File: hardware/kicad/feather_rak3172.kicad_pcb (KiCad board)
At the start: 2 copper layers, 51 x 23.1 mm, 51 parts, among them J1 Pin Header, J2 Pin Header, J3 USB_C_Receptacle_USB2.0, J4 915MHz SMA, J5 SWD, J6 JST-2PH, Q1 DMG341, SW1 RESET, SW2 BOOT, U1 RAK3172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

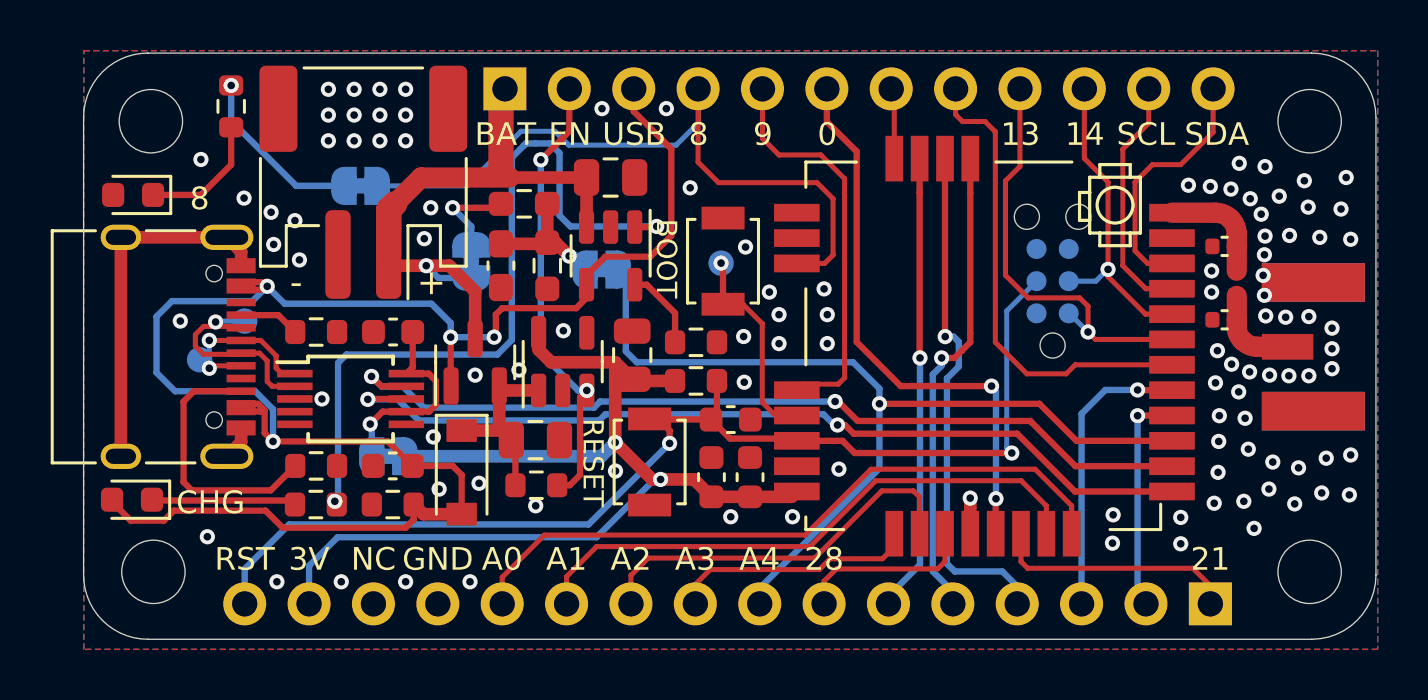
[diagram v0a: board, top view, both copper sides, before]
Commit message: minor traces adjustment
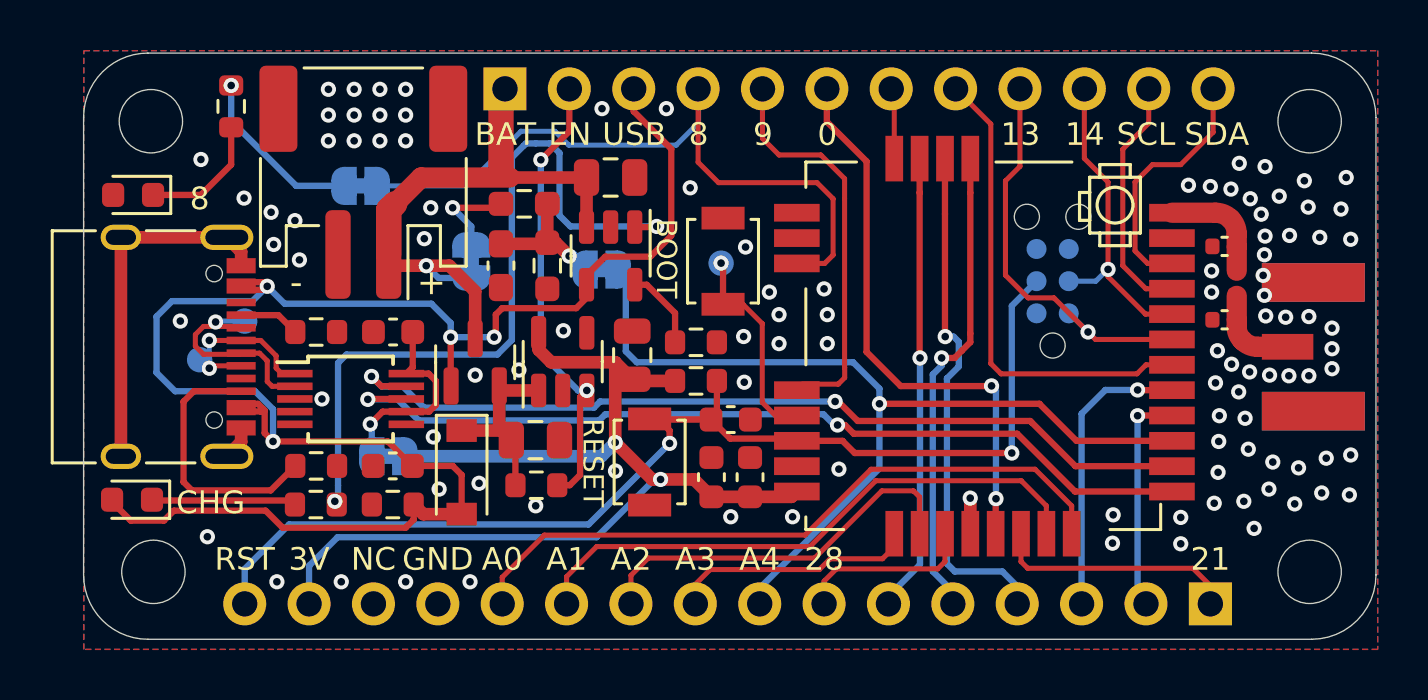
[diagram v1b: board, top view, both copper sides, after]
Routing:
- net /PA13: track 16.9 -> 16.3 mm
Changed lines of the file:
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@@
   (via (at 139.954 106.172) (size 0.6) (drill 0.3) (layers "F.Cu" "B.Cu") (net 13))
   (via (at 153.4563 106.553) (size 0.6) (drill 0.3) (layers "F.Cu" "B.Cu") (net 13))
-  (segment (start 153.25632 100.94688) (end 153.25632 106.35302) (width 0.2) (layer "B.Cu") (net 13))
+  (segment (start 153.4563 106.553) (end 153.4563 100.7469) (width 0.25) (layer "B.Cu") (net 13))
   (segment (start 124.94452 109.37048) (end 123.19 111.125) (width 0.25) (layer "B.Cu") (net 13))
-  (segment (start 154.432 99.7712) (end 153.25632 100.94688) (width 0.2) (layer "B.Cu") (net 13))
   (segment (start 123.19 111.125) (end 123.19 112.503949) (width 0.25) (layer "B.Cu") (net 13))
   (segment (start 139.954 106.172) (end 136.75552 109.37048) (width 0.25) (layer "B.Cu") (net 13))
   (segment (start 136.75552 109.37048) (end 124.94452 109.37048) (width 0.25) (layer "B.Cu") (net 13))
-  (segment (start 153.25632 106.35302) (end 153.4563 106.553) (width 0.2) (layer "B.Cu") (net 13))
+  (segment (start 153.4563 100.7469) (end 154.432 99.7712) (width 0.25) (layer "B.Cu") (net 13))
   (segment (start 162.3314 101.5873) (end 162.3314 101.31316) (width 0.8) (layer "F.Cu") (net 14))
   (segment (start 163.155249 102.362) (end 164.338 102.362) (width 0.8) (layer "F.Cu") (net 14))
@@
   (segment (start 157.0736 99.4706) (end 157.090399 99.4706) (width 0.2) (layer "B.Cu") (net 43))
   (segment (start 157.090399 99.4706) (end 157.253999 99.307) (width 0.2) (layer "B.Cu") (net 43))
+  (segment (start 156.464 101.7778) (end 155.1178 100.4316) (width 0.2) (layer "F.Cu") (net 44))
   (segment (start 156.464 101.7778) (end 156.7578 102.0716) (width 0.2) (layer "F.Cu") (net 44))
+  (segment (start 154.1018 100.4316) (end 153.206179 99.535979) (width 0.2) (layer "F.Cu") (net 44))
+  (segment (start 153.778949 95.242651) (end 153.778949 92.183949) (width 0.2) (layer "F.Cu") (net 44))
   (segment (start 153.206179 95.815421) (end 153.778949 95.242651) (width 0.2) (layer "F.Cu") (net 44))
-  (segment (start 153.206179 99.535979) (end 153.206179 99.358179) (width 0.2) (layer "F.Cu") (net 44))
-  (segment (start 156.464 100.7618) (end 156.1338 100.4316) (width 0.2) (layer "F.Cu") (net 44))
-  (segment (start 154.1018 100.4316) (end 153.206179 99.535979) (width 0.2) (layer "F.Cu") (net 44))
-  (segment (start 156.1338 100.4316) (end 154.1018 100.4316) (width 0.2) (layer "F.Cu") (net 44))
   (segment (start 156.7578 102.0716) (end 159.7746 102.0716) (width 0.2) (layer "F.Cu") (net 44))
-  (segment (start 156.464 101.7778) (end 156.464 100.7618) (width 0.2) (layer "F.Cu") (net 44))
-  (segment (start 153.206179 99.358179) (end 153.206179 95.815421) (width 0.2) (layer "F.Cu") (net 44))
-  (segment (start 153.778949 95.242651) (end 153.778949 92.183949) (width 0.2) (layer "F.Cu") (net 44))
+  (segment (start 153.206179 99.535979) (end 153.206179 95.815421) (width 0.2) (layer "F.Cu") (net 44))
+  (segment (start 155.1178 100.4316) (end 154.1018 100.4316) (width 0.2) (layer "F.Cu") (net 44))
   (via (at 156.464 101.7778) (size 0.6) (drill 0.3) (layers "F.Cu" "B.Cu") (net 44))
   (segment (start 155.7274 101.0412) (end 156.464 101.7778) (width 0.2) (layer "B.Cu") (net 44))
@@
   (segment (start 154.0826 111.0996) (end 160.6042 111.0996) (width 0.2) (layer "F.Cu") (net 47))
   (segment (start 160.6042 111.0996) (end 161.29 111.7854) (width 0.2) (layer "F.Cu") (net 47))
-  (segment (start 155.6004 103.4288) (end 154.051 103.4288) (width 0.2) (layer "F.Cu") (net 48))
-  (segment (start 151.511 93.472) (end 151.238949 93.199949) (width 0.2) (layer "F.Cu") (net 48))
-  (segment (start 152.806659 93.878659) (end 152.4 93.472) (width 0.2) (layer "F.Cu") (net 48))
-  (segment (start 152.806659 102.184459) (end 152.806659 93.878659) (width 0.2) (layer "F.Cu") (net 48))
-  (segment (start 154.051 103.4288) (end 152.806659 102.184459) (width 0.2) (layer "F.Cu") (net 48))
-  (segment (start 155.9576 103.0716) (end 155.6004 103.4288) (width 0.2) (layer "F.Cu") (net 48))
-  (segment (start 152.4 93.472) (end 151.511 93.472) (width 0.2) (layer "F.Cu") (net 48))
-  (segment (start 159.7746 103.0716) (end 155.9576 103.0716) (width 0.2) (layer "F.Cu") (net 48))
-  (segment (start 151.238949 93.199949) (end 151.238949 92.183949) (width 0.2) (layer "F.Cu") (net 48))
+  (segment (start 152.6286 93.5736) (end 151.238949 92.183949) (width 0.2) (layer "F.Cu") (net 48))
+  (segment (start 152.6286 103.0224) (end 152.6286 93.5736) (width 0.2) (layer "F.Cu") (net 48))
+  (segment (start 158.7516 103.0716) (end 158.3944 103.4288) (width 0.2) (layer "F.Cu") (net 48))
+  (segment (start 153.035 103.4288) (end 152.6286 103.0224) (width 0.2) (layer "F.Cu") (net 48))
+  (segment (start 159.7746 103.0716) (end 158.7516 103.0716) (width 0.2) (layer "F.Cu") (net 48))
+  (segment (start 158.3944 103.4288) (end 153.035 103.4288) (width 0.2) (layer "F.Cu") (net 48))
   (segment (start 148.8196 92.3046) (end 148.698949 92.183949) (width 0.2) (layer "F.Cu") (net 49))
   (segment (start 148.8196 94.9366) (end 148.8196 92.3046) (width 0.2) (layer "F.Cu") (net 49))
-  (segment (start 147.33764 102.17644) (end 149.0726 103.9114) (width 0.25) (layer "F.Cu") (net 50))
-  (segment (start 147.33764 94.65804) (end 147.33764 102.17644) (width 0.25) (layer "F.Cu") (net 50))
+  (segment (start 152.648133 103.9114) (end 149.0726 103.9114) (width 0.25) (layer "F.Cu") (net 50))
   (segment (start 152.8196 109.7366) (end 152.8196 108.3686) (width 0.25) (layer "F.Cu") (net 50))
+  (segment (start 149.0726 103.9114) (end 147.7264 102.5652) (width 0.25) (layer "F.Cu") (net 50))
+  (segment (start 146.158949 93.479349) (end 146.158949 92.183949) (width 0.25) (layer "F.Cu") (net 50))
   (segment (start 152.8196 108.3686) (end 152.8318 108.3564) (width 0.25) (layer "F.Cu") (net 50))
-  (segment (start 146.158949 92.183949) (end 146.158949 93.479349) (width 0.25) (layer "F.Cu") (net 50))
-  (segment (start 146.158949 93.479349) (end 147.33764 94.65804) (width 0.25) (layer "F.Cu") (net 50))
-  (segment (start 149.0726 103.9114) (end 152.65682 103.9114) (width 0.25) (layer "F.Cu") (net 50))
-  (via (at 152.65682 103.9114) (size 0.6) (drill 0.3) (layers "F.Cu" "B.Cu") (net 50))
+  (segment (start 152.65682 103.902713) (end 152.648133 103.9114) (width 0.25) (layer "F.Cu") (net 50))
+  (segment (start 147.7264 95.0468) (end 146.158949 93.479349) (width 0.25) (layer "F.Cu") (net 50))
+  (segment (start 147.7264 102.5652) (end 147.7264 95.0468) (width 0.25) (layer "F.Cu") (net 50))
+  (via (at 152.65682 103.902713) (size 0.6) (drill 0.3) (layers "F.Cu" "B.Cu") (net 50))
   (via (at 152.8318 108.3564) (size 0.6) (drill 0.3) (layers "F.Cu" "B.Cu") (net 50))
-  (segment (start 152.8318 104.08638) (end 152.65682 103.9114) (width 0.25) (layer "B.Cu") (net 50))
-  (segment (start 152.8318 108.3564) (end 152.8318 104.08638) (width 0.25) (layer "B.Cu") (net 50))
+  (segment (start 152.8318 104.077693) (end 152.8318 108.3564) (width 0.25) (layer "B.Cu") (net 50))
+  (segment (start 152.65682 103.902713) (end 152.8318 104.077693) (width 0.25) (layer "B.Cu") (net 50))
   (segment (start 146.8628 103.5812) (end 146.6088 103.8352) (width 0.2) (layer "F.Cu") (net 51))
   (segment (start 146.8628 103.18216) (end 146.8628 103.5812) (width 0.2) (layer "F.Cu") (net 51))

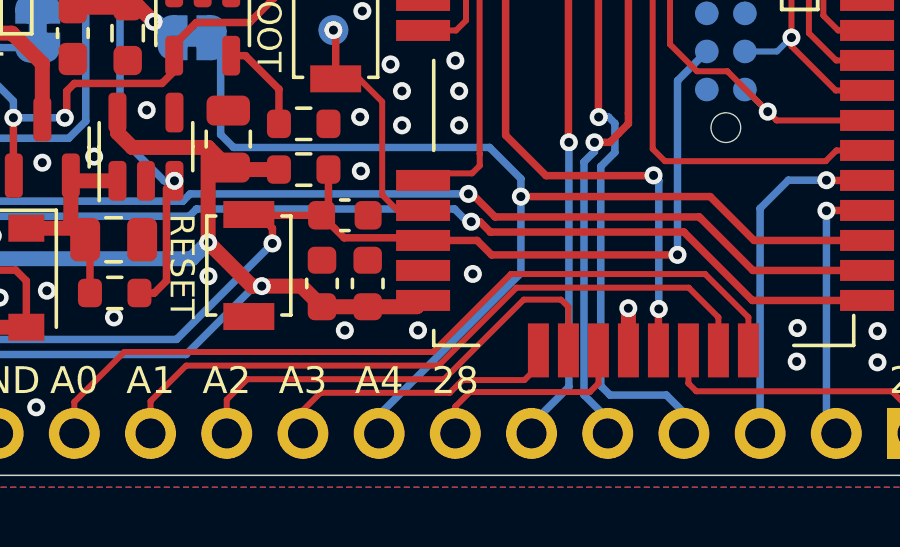
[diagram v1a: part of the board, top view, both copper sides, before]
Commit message: minor trace adjustment
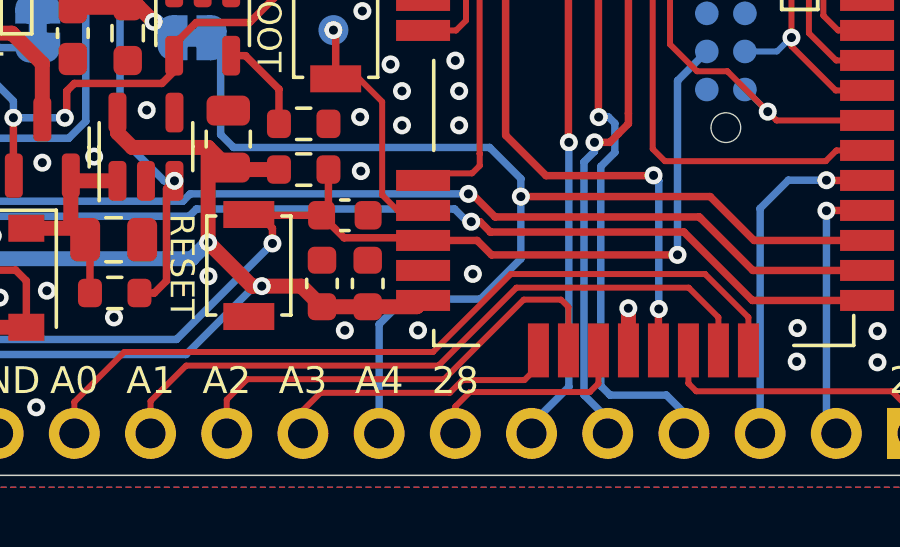
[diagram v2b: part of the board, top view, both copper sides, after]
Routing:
- net /A4: track 36.6 -> 38.1 mm
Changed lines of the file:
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@@
   (segment (start 148.2344 104.60898) (end 154.54538 104.60898) (width 0.25) (layer "F.Cu") (net 7))
   (via (at 148.2344 104.60898) (size 0.6) (drill 0.3) (layers "F.Cu" "B.Cu") (net 7))
+  (segment (start 146.8882 108.0262) (end 144.3482 108.0262) (width 0.25) (layer "B.Cu") (net 7))
   (segment (start 138.6586 102.9716) (end 147.193 102.9716) (width 0.25) (layer "B.Cu") (net 7))
   (segment (start 148.2344 104.013) (end 148.2344 104.60898) (width 0.25) (layer "B.Cu") (net 7))
   (segment (start 137.922 99.314) (end 138.2268 99.6188) (width 0.25) (layer "B.Cu") (net 7))
+  (segment (start 143.51 108.8644) (end 143.51 112.503949) (width 0.25) (layer "B.Cu") (net 7))
+  (segment (start 148.2344 106.68) (end 146.8882 108.0262) (width 0.25) (layer "B.Cu") (net 7))
+  (segment (start 148.2344 104.60898) (end 148.2344 106.68) (width 0.25) (layer "B.Cu") (net 7))
   (segment (start 138.2268 99.6188) (end 138.2268 102.5398) (width 0.25) (layer "B.Cu") (net 7))
-  (segment (start 143.51 112.503949) (end 143.51 111.887) (width 0.25) (layer "B.Cu") (net 7))
   (segment (start 147.193 102.9716) (end 148.2344 104.013) (width 0.25) (layer "B.Cu") (net 7))
   (segment (start 138.2268 102.5398) (end 138.6586 102.9716) (width 0.25) (layer "B.Cu") (net 7))
-  (segment (start 148.2344 107.1626) (end 148.2344 104.60898) (width 0.25) (layer "B.Cu") (net 7))
-  (segment (start 143.51 111.887) (end 148.2344 107.1626) (width 0.25) (layer "B.Cu") (net 7))
+  (segment (start 144.3482 108.0262) (end 143.51 108.8644) (width 0.25) (layer "B.Cu") (net 7))
   (segment (start 145.865826 111.1504) (end 146.290745 110.725481) (width 0.2) (layer "F.Cu") (net 8))
   (segment (start 140.97 111.7346) (end 141.5542 111.1504) (width 0.2) (layer "F.Cu") (net 8))

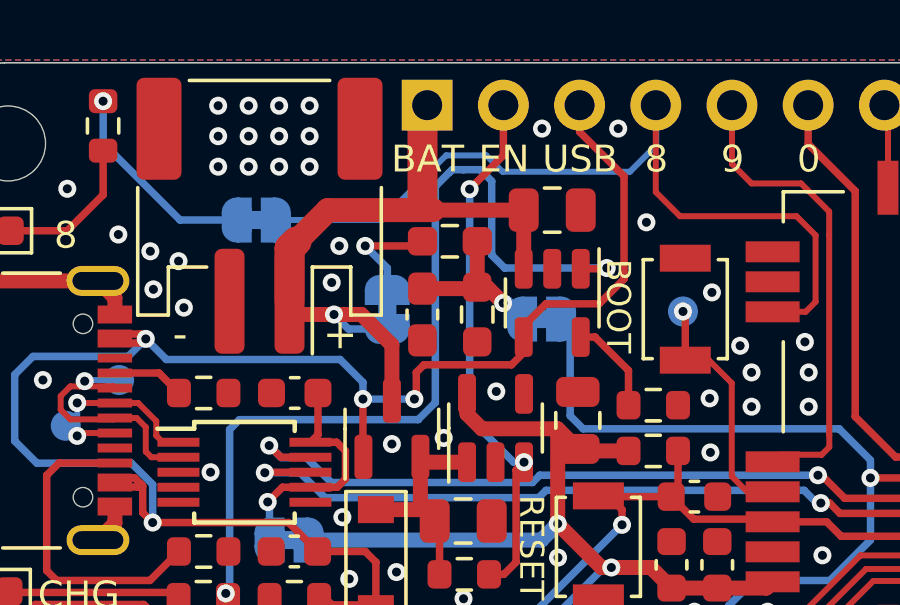
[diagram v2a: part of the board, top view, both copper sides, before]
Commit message: add component description and minor footprint changes
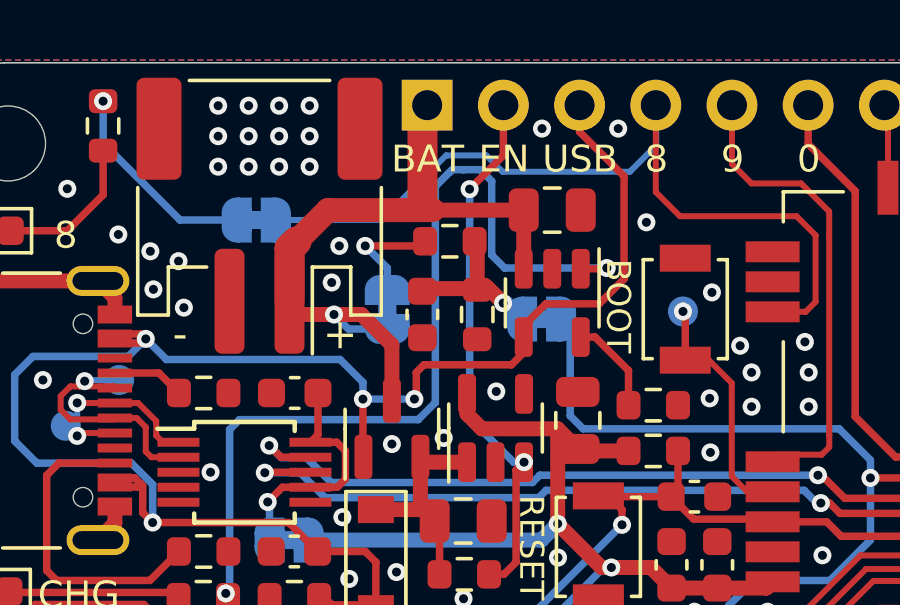
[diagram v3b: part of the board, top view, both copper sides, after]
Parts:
- C1, C4, C7: value 0.1uF -> 100nF
- C11: footprint Capacitor_SMD:C_0603_1608Metric_Pad1.08x0.95mm_HandSolder -> Capacitor_SMD:C_0603_1608Metric
- D3: value MBR0540 -> B5819W
- R10, R9: footprint Resistor_SMD:R_0603_1608Metric_Pad0.98x0.95mm_HandSolder -> Resistor_SMD:R_0603_1608Metric
- R6: value 10K -> 1K
- U3: value MCP73831-2-OT -> MCP73831T-2ACI/OT
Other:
- board text added: "Rev 4.4"
- board text removed: "Rev 4"
